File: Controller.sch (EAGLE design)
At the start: 35 parts, among them SW1 MULTICOLOR_BUTTON, SW10 MY_LBR_SPSTSWITCH, SW2 MULTICOLOR_BUTTON, SW3 MULTICOLOR_BUTTON, SW4 MULTICOLOR_BUTTON, SW5 MULTICOLOR_BUTTON, SW6 MULTICOLOR_BUTTON, SW7 MULTICOLOR_BUTTON, SW8 MULTICOLOR_BUTTON, SW9 MY_LBR_SPSTSWITCH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

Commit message: Redoing the board
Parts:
- removed R20, R21, R22, R23: 1k, rcl:R-US_R1206
- removed R24, R25: 10k, rcl:R-US_R1206
- removed R26: 100k, rcl:R-US_R1206
- removed SW10, SW9: MY_LBR_SPSTSWITCH, Controller:MY_LBR_SPSTSWITCH
- removed U$2, U$3: BUMPER_BUMPER, Controller:BUMPER_BUMPER
- added C1, C2, C9: 0.1u, rcl:C-USC1206
- added C4, C6: 22p, rcl:C-USC1206
- added C7: 10u, rcl:C-USC1206
- added C8: 10U, rcl:C-USC1206
- added Q1: (no value), crystal:CRYSTALHC49S
- added R1, R2, R3, R4: 100k, rcl:R-US_R1206
- added U3: DRV5053VAQLPGM, Controller:DRV5053VAQLPGM
- added U4: LM1086IT-3.3/NOPB, Controller:LM1086IT-3.3/NOPB
- C3: value 10uF -> 0.1u
- C5: value 22pF -> 0.1u
- U2: value MCP6002T-I/SNSOIC8-N_MC-M -> DRV5053VAQLPGM; device Controller:MCP6002T-I/SNSOIC8-N_MC-M -> Controller:DRV5053VAQLPGM
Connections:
- removed net LEFT_BUTTON_OUTPUT: C5.1, R26.1, U2.VINA+
- removed net LEFT_OUTPUT: U2.VINA-, U2.VOUTA
- removed net N$13: R21.1, R22.2, U$3.IN
- removed net N$18: R22.1, R23.2, SW9.P$1
- removed net N$19: R23.1, R24.2, SW10.P$1
- removed net N$2: R20.1, R21.2, U$2.IN
- removed net N$20: R24.1, R25.2
- removed net N$21: R26.2, SW10.P$2, SW9.P$2, U$2.OUT, U$3.OUT
- removed net N$24: U1.PC1/ADC1/PCINT9
- removed net N$25: U1.PC0/ADC0/PCINT8
- removed net N$5: S1.SEL+, S2.SEL+, U$4.IN, U$6.IN
- removed net RIGHT_BUTTON_OUTPUT: U2.VINB+
- removed net RIGHT_OUTPUT: U2.VINB-, U2.VOUTB
- new net $NC2: S2.SEL-, SW2.P$4, SW6.P$4
- new net N$C1: C1.1, R1.1, S1.SEL-, SW1.P$4, SW5.P$4
- new net N$C2: C2.1, R2.1
- new net N$C3: C3.1, R3.1, SW3.P$4, SW7.P$4, U$4.OUT
- new net N$C4: C5.1, R4.1, SW4.P$4, SW8.P$4, U$6.OUT
- new net R1: SW1.P$1, SW2.P$1, SW3.P$1, SW4.P$1, U1.PB3/MOSI/OC2A/PCINT3
- new net R2: SW5.P$1, SW6.P$1, SW7.P$1, SW8.P$1, U1.PB2/!SS/OC1B/PCINT2
- new net R3: S1.SEL+, S2.SEL+, U$4.IN, U$6.IN, U1.PB1/OC1A/PCINT1
- new net TRIGGER_LEFT: U1.PC1/ADC1/PCINT9, U2.OUT
- new net TRIGGER_RIGHT: U1.PC0/ADC0/PCINT8, U3.OUT
- net +3V3: now also C7.1, C9.1, U4.VOUT
- net +5V: now also C8.1, U2.VCC, U3.VCC, U4.VIN; no longer C3.1, R20.2, U2.VDD
- net C1: now also R1.2, U1.PCINT18/INT0/PD2; no longer S1.SEL-, SW1.P$4, SW5.P$4
- net C2: now also R2.2, U1.PCINT19/OC2B/INT1/PD3; no longer S2.SEL-, SW2.P$4, SW6.P$4
- net C3: now also R3.2, U1.PCINT21/OC0B/T1/PD5; no longer SW3.P$4, SW7.P$4, U$4.GROUND
- net C4: now also R4.2, U1.PCINT0/CLKO/ICP1/PB0; no longer SW4.P$4, SW8.P$4, U$6.GROUND
- net GND: now also C1.2, C2.2, C4.2, C6.2, C7.2, C8.2, C9.2, U2.GND, U3.GND, U4.ADJ/GND; no longer R25.1, U$2.GROUND, U$2.GROUND1, U$3.GROUND, U$3.GROUND1, U2.VSS
- net N$3: now also C4.1, Q1.1, U1.PCINT6/XTAL1/TOSC1/PB6; no longer SW1.P$1, SW2.P$1, SW3.P$1, SW4.P$1
- net N$4: now also C6.1, Q1.2, U1.PCINT7/XTAL2/TOSC2/PB7; no longer SW5.P$1, SW6.P$1, SW7.P$1, SW8.P$1

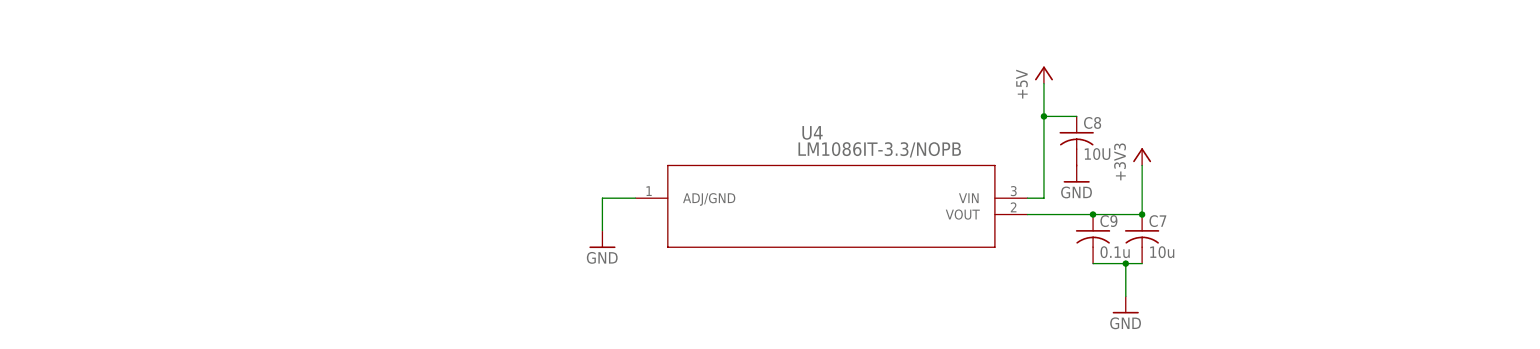
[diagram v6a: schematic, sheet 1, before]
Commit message: added 5V regulator
Still need to add BMS circuitry and switch
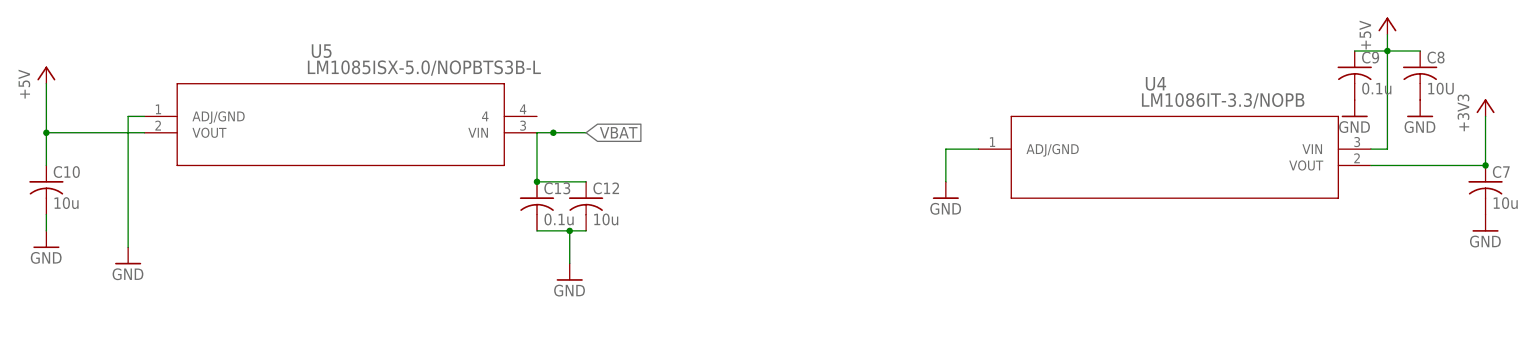
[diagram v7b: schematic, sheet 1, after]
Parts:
- added C10, C12: 10u, rcl:C-USC1206
- added C13: 0.1u, rcl:C-USC1206
- added U5: LM1085ISX-5.0/NOPBTS3B-L, Controller:LM1085ISX-5.0/NOPBTS3B-L
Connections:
- new net VBAT: C12.1, C13.1, U5.VIN
- net +3V3: no longer C9.1
- net +5V: now also C10.1, C9.1, U5.VOUT
- net GND: now also C10.2, C12.2, C13.2, U5.ADJ/GND
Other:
- moved on the sheet: C7, C8, C9, U4

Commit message: rerouted so we only have 2 layers, added PWM pin
Need to add battery switch,indicator Vbat pins
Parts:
- added C11: 0.1u, rcl:C-USC1206
- added R5, R6: 100k, rcl:R-US_R1206
- C5: value 0.1u -> 10U
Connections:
- removed net $NC2: S2.SEL-, SW2.P$4, SW6.P$4
- removed net C4: R4.2, U1.PCINT0/CLKO/ICP1/PB0
- removed net N$C1: C1.1, R1.1, S1.SEL-, SW1.P$4, SW5.P$4
- removed net N$C4: C5.1, R4.1, SW4.P$4, SW8.P$4, U$6.OUT
- new net $NC1: C1.1, R1.1, R4.1, SW1.P$4, SW2.P$4, SW5.P$4, SW6.P$4
- new net PWM: U1.PCINT22/OC0A/AIN0/PD6
- new net R4: S2.SEL+, SW6.P$1, SW8.P$1, U1.PB3/MOSI/OC2A/PCINT3
- net +3V3: now also C11.1, C5.1
- net +5V: now also U1.AREF, U1.AVCC
- net GND: now also C11.2, R4.2, R5.2, R6.2
- net N$C2: now also R5.1, SW3.P$4, SW4.P$4, SW7.P$4, SW8.P$4
- net N$C3: now also R6.1, S1.SEL-, S2.SEL-, U$6.OUT; no longer SW3.P$4, SW7.P$4
- net R1: now also U$4.IN, U1.PCINT0/CLKO/ICP1/PB0; no longer SW2.P$1, SW4.P$1, U1.PB3/MOSI/OC2A/PCINT3
- net R2: now also U$6.IN, U1.PB1/OC1A/PCINT1; no longer SW6.P$1, SW8.P$1, U1.PB2/!SS/OC1B/PCINT2
- net R3: now also SW2.P$1, SW4.P$1, U1.PB2/!SS/OC1B/PCINT2; no longer S2.SEL+, U$4.IN, U$6.IN, U1.PB1/OC1A/PCINT1
- net RX: now also U1.PCINT16/RXD/PD0
- net TX: now also U1.PCINT17/TXD/PD1
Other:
- moved on the sheet: C1, C2, C3, R1, R2, R3, R4, S1, S2, SW2, SW3, SW4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
